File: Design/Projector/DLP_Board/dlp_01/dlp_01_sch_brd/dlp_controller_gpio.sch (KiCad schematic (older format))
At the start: 16 parts

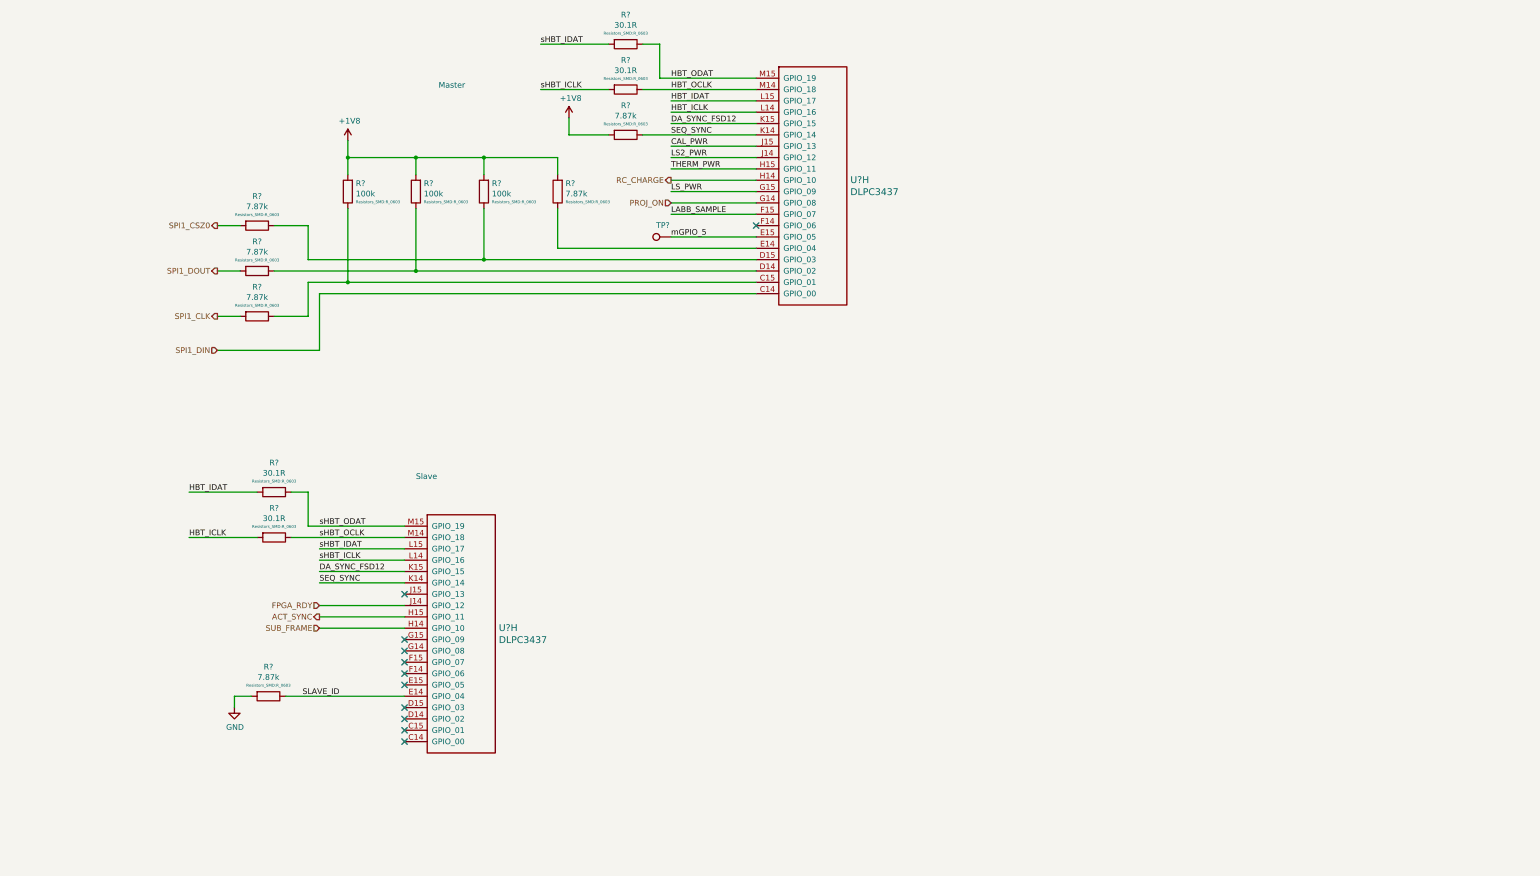
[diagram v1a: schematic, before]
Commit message: Initial placement of power converters, BGA fanout and Z-turn board outline imported
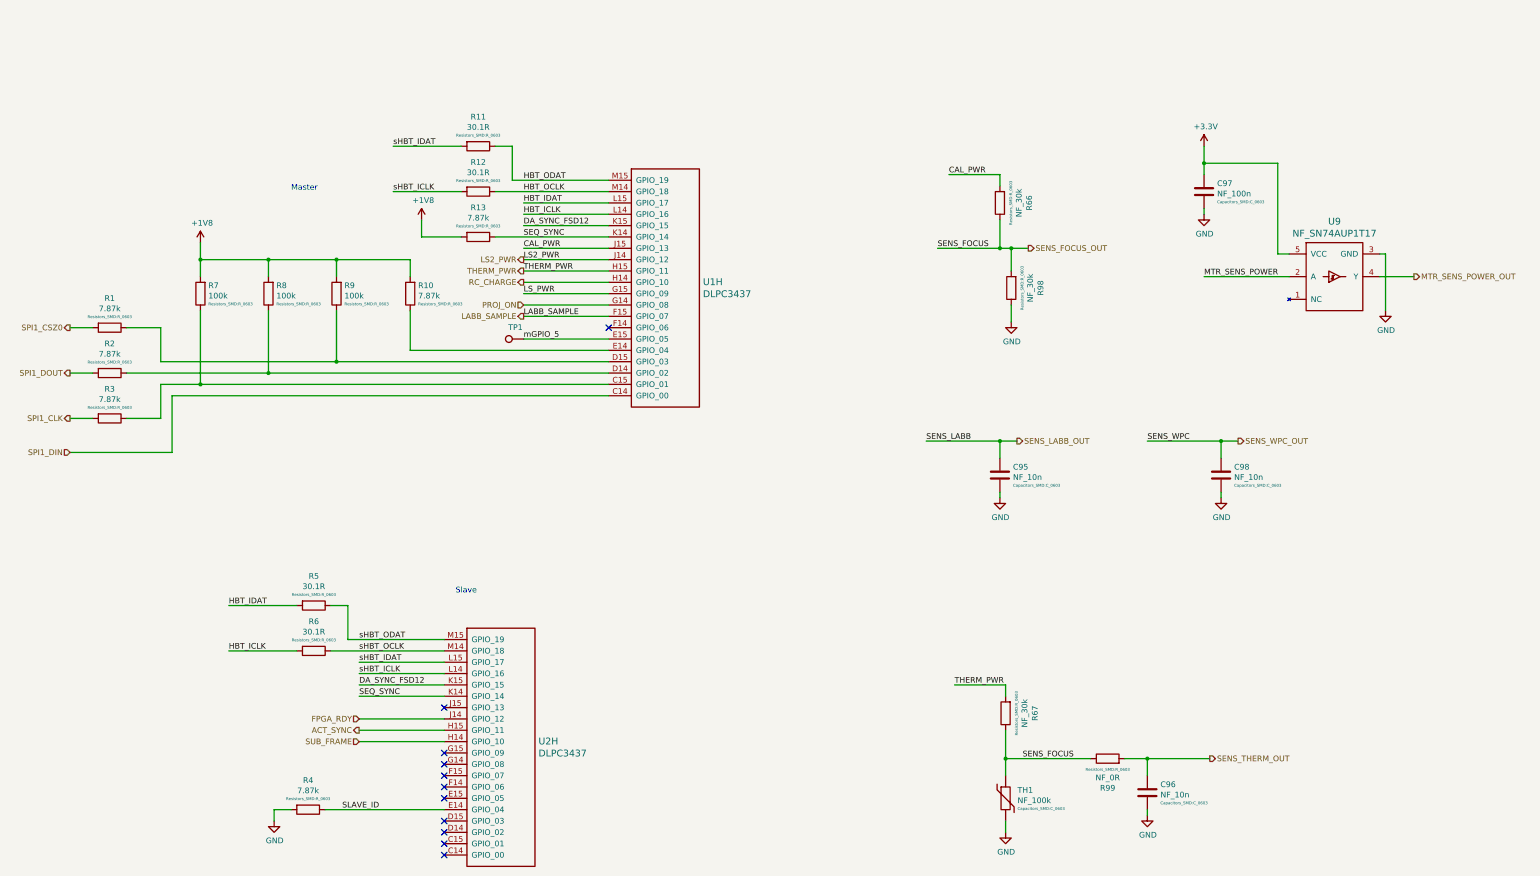
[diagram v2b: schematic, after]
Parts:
- added C95, C96, C98: NF_10n, Capacitors_SMD:C_0603, symbol Device:C
- added C97: NF_100n, Capacitors_SMD:C_0603, symbol Device:C
- added R66, R67, R98: NF_30k, Resistors_SMD:R_0603, symbol Device:R
- added R99: NF_0R, Resistors_SMD:R_0603, symbol Device:R
- added TH1: NF_100k, Capacitors_SMD:C_0603, symbol Device:Thermistor
- added U9: NF_SN74AUP1T17, SC-70-5:SC-70-5, symbol RocketScreamKicadLibrary:SN74AUP1T17
- gave numbers to parts that had none: 16
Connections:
- net CAL_PWR: now also R66.2
- net GND: now also C95.2, C96.2, C97.2, C98.2, R98.1, TH1.2, U9.3 (GND)
- net THERM_PWR: now also R67.2
- new net +3V3: C97.1, U9.5 (VCC)
- new net MTR_SENS_POWER: U9.2 (A)
- new net MTR_SENS_POWER_OUT: U9.4 (Y)
- new net SENS_FOCUS_OUT: R66.1, R67.1, R98.2, R99.1, TH1.1
- new net SENS_LABB_OUT: C95.1
- new net SENS_THERM_OUT: C96.1, R99.2
- new net SENS_WPC_OUT: C98.1
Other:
- moved on the sheet: R1, R10, R11, R12, R13, R2, R3, R4, R5, R6, R7, R8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
